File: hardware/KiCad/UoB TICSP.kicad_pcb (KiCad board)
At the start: 4 copper layers, 80 x 40 mm, 57 parts, among them J1 Wago 233-503, J2 SMA, J3 PT02A12-4PW, J4 Wago 233-506, U1 LT3045EDD, U2 LT3094EDD, U3 OPA818IDRG, U4 OPA1632DGN, U5 LT3045EDD

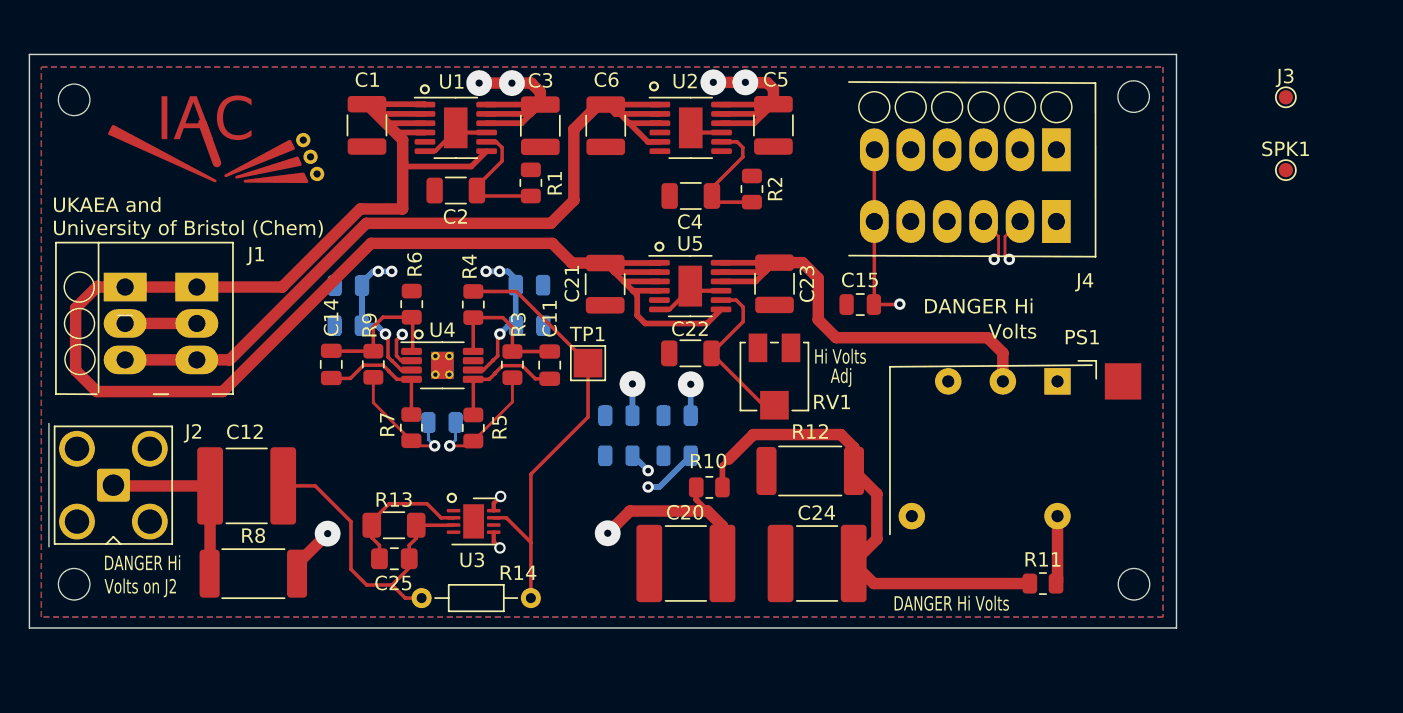
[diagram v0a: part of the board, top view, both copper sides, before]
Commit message: End of day save. Just needs voids added to planes to reduce capacitance
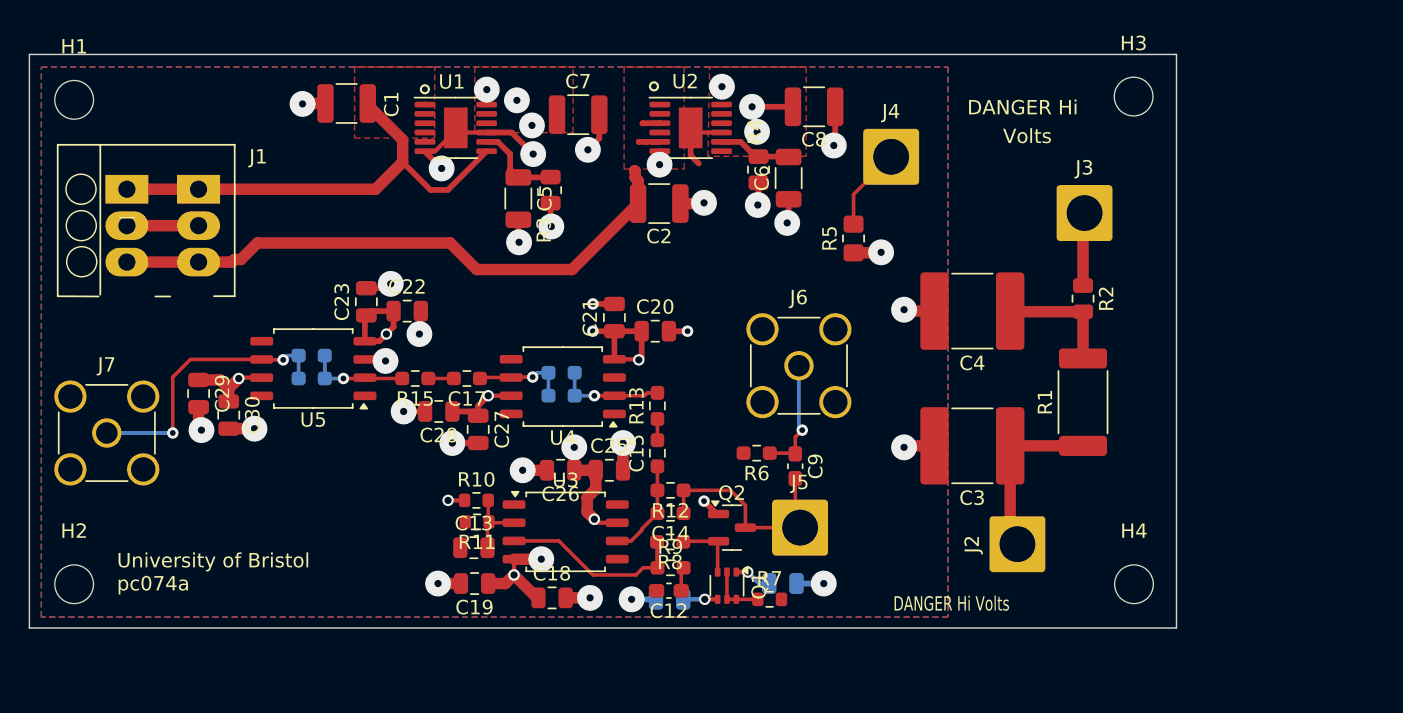
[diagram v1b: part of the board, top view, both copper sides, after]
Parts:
- removed IAC: IAC Logo, UoB Cremat Library:IAC Logo
- removed PS1: XP-Q25-5, UoB Cremat Library:XP-Q25-5 DCtoHDC
- removed RV1: 50k 3314J-2-503E, Potentiometer_SMD:Potentiometer_Bourns_3314J_Vertical
- removed SPK1: SPS-2220-03, TestPoint:TestPoint_Pad_D1.0mm
- removed TP1: TestPoint, TestPoint:TestPoint_Pad_2.0x2.0mm
- added C26: 10uF, Capacitor_SMD:C_0805_2012Metric, F.Cu at (121.0, 84.0)
- added C27: 0.1uF, Capacitor_SMD:C_0805_2012Metric, F.Cu at (115.3, 81.2)
- added C28: 10uF, Capacitor_SMD:C_0805_2012Metric, F.Cu at (112.5, 79.9)
- added C29: 0.1uF, Capacitor_SMD:C_0805_2012Metric, F.Cu at (95.8, 78.7)
- added C30: 10uF, Capacitor_SMD:C_0805_2012Metric, F.Cu at (97.9, 80.2)
- added J5: Conn_01x01_Pin, Connector_Wire:SolderWire-2sqmm_1x01_D2mm_OD3.9mm, F.Cu at (137.8, 88.0)
- added J6: SMA, Connector_Coaxial:SMA_Amphenol_901-144_Vertical, F.Cu at (137.7, 76.7)
- added J7: SMA, Connector_Coaxial:SMA_Amphenol_901-144_Vertical, F.Cu at (89.4, 81.4)
- added Q1: MMDT3906, Package_TO_SOT_SMD:SOT-363_SC-70-6, F.Cu at (132.7, 92.0)
- added Q2: 2SK932, Package_TO_SOT_SMD:SOT-23, F.Cu at (133.0, 88.0)
- added R15: 510, Resistor_SMD:R_0603_1608Metric_Pad0.98x0.95mm_HandSolder, F.Cu at (110.9, 77.6)
- added R16: 10k, Resistor_SMD:R_0603_1608Metric_Pad0.98x0.95mm_HandSolder, B.Cu at (103.7, 76.0)
- C11: value 1nF -> 10uF; moved to B.Cu
- C12: value 0.01uF C2220C103KHRACTU -> 1nF; footprint Capacitor_SMD:C_2220_5650Metric -> Capacitor_SMD:C_0603_1608Metric_Pad1.08x0.95mm_HandSolder
- C13: value 2.7nF -> 0.1uF; moved to F.Cu
- C14: value 1nF -> 10p; footprint Capacitor_SMD:C_0805_2012Metric -> Resistor_SMD:R_0603_1608Metric_Pad0.98x0.95mm_HandSolder
- C15: value 0.1uF -> 1n; footprint Capacitor_SMD:C_0805_2012Metric -> Resistor_SMD:R_0603_1608Metric_Pad0.98x0.95mm_HandSolder
- C16: value 10uF -> 50p; footprint Capacitor_SMD:C_0805_2012Metric -> Resistor_SMD:R_0603_1608Metric_Pad0.98x0.95mm_HandSolder
- C17: value 10uF -> 1n; footprint Capacitor_SMD:C_0805_2012Metric -> Resistor_SMD:R_0603_1608Metric_Pad0.98x0.95mm_HandSolder; moved to F.Cu
- C18: moved to F.Cu
- C19: value 0.1uF -> 10uF; moved to F.Cu
- C2: value 0.47uF -> 10uF C1210C106K3PACTU; footprint Capacitor_SMD:C_1206_3216Metric -> Capacitor_SMD:C_1210_3225Metric
- C20: value 0.01uF C2220C103KHRACTU -> 0.1uF; footprint Capacitor_SMD:C_2220_5650Metric -> Capacitor_SMD:C_0805_2012Metric
- C21, C23: value 10uF C1210C106K3PACTU -> 10uF; footprint Capacitor_SMD:C_1210_3225Metric -> Capacitor_SMD:C_0805_2012Metric
- C22: value 0.47uF -> 0.1uF; footprint Capacitor_SMD:C_1206_3216Metric -> Capacitor_SMD:C_0805_2012Metric
- C24: value 0.01uF C2220C103KHRACTU -> 50p; footprint Capacitor_SMD:C_2220_5650Metric -> Resistor_SMD:R_0603_1608Metric_Pad0.98x0.95mm_HandSolder; moved to B.Cu
- C25: value 0.5pF CQ0805BRNPO0BNR50 -> 0.1uF; footprint Capacitor_SMD:C_0805_2012Metric_Pad1.18x1.45mm_HandSolder -> Capacitor_SMD:C_0805_2012Metric
- C3: value 10uF C1210C106K3PACTU -> 0.01uF C2220C103KHRACTU; footprint Capacitor_SMD:C_1210_3225Metric -> Capacitor_SMD:C_2220_5750Metric_Pad1.97x5.40mm_HandSolder
- C4: value 4.7uF -> 0.01uF C2220C103KHRACTU; footprint Capacitor_SMD:C_1206_3216Metric -> Capacitor_SMD:C_2220_5750Metric_Pad1.97x5.40mm_HandSolder
- C5: value 10uF C1210C106K3PACTU -> 0.47uF; footprint Capacitor_SMD:C_1210_3225Metric -> Capacitor_SMD:C_1206_3216Metric
- C6: value 10uF C1210C106K3PACTU -> 4.7uF; footprint Capacitor_SMD:C_1210_3225Metric -> Capacitor_SMD:C_1206_3216Metric
- C7: value 10uF -> 10uF C1210C106K3PACTU; footprint Capacitor_SMD:C_0805_2012Metric -> Capacitor_SMD:C_1210_3225Metric; moved to F.Cu
- C8: value 0.1uF -> 10uF C1210C106K3PACTU; footprint Capacitor_SMD:C_0805_2012Metric -> Capacitor_SMD:C_1210_3225Metric; moved to F.Cu
- C9: value 10uF -> 1pF; footprint Capacitor_SMD:C_0805_2012Metric -> Capacitor_SMD:C_0603_1608Metric_Pad1.08x0.95mm_HandSolder; moved to F.Cu
- H1, H2, H3, H4: footprint MountingHole:MountingHole_2.2mm_M2_DIN965 -> MountingHole:MountingHole_2.7mm_M2.5
- J2: value SMA -> Conn_01x01_Pin; footprint Connector_Coaxial:SMA_Amphenol_901-143_Horizontal -> Connector_Wire:SolderWire-2sqmm_1x01_D2mm_OD3.9mm
- J3: value PT02A12-4PW -> Conn_01x01_Pin; footprint TestPoint:TestPoint_Pad_D1.0mm -> Connector_Wire:SolderWire-2sqmm_1x01_D2mm_OD3.9mm
- J4: value Wago 233-506 -> Conn_01x01_Pin; footprint UoB Cremat Library:TerminalBlock_WAGO_233-506_1x06_P2.54mm_45Degree -> Connector_Wire:SolderWire-2sqmm_1x01_D2mm_OD3.9mm
- R1: value 60k -> 200M CRHA2510AF200MFKEF; footprint Resistor_SMD:R_0805_2012Metric -> Resistor_SMD:R_2512_6332Metric_Pad1.40x3.35mm_HandSolder
- R10: value 10M RCV080510M0FKEA -> 1k; footprint Resistor_SMD:R_0805_2012Metric -> Resistor_SMD:R_0603_1608Metric
- R11: value 1 KTR10EZPF1R00 -> 1k; footprint Resistor_SMD:R_0805_2012Metric -> Resistor_SMD:R_0603_1608Metric
- R12: value 200M CRHA2510AF200MFKEF -> 2.2M; footprint Resistor_SMD:R_2512_6332Metric_Pad1.40x3.35mm_HandSolder -> Resistor_SMD:R_0603_1608Metric_Pad0.98x0.95mm_HandSolder
- R13: value 100M CRCW1206100MJPEAHR -> 510; footprint Resistor_SMD:R_1206_3216Metric_Pad1.30x1.75mm_HandSolder -> Resistor_SMD:R_0603_1608Metric_Pad0.98x0.95mm_HandSolder
- R14: value nf -> 10k; footprint Resistor_THT:R_Axial_DIN0204_L3.6mm_D1.6mm_P7.62mm_Horizontal -> Resistor_SMD:R_0603_1608Metric_Pad0.98x0.95mm_HandSolder; moved to B.Cu
- R2: value 60k -> 10M RCV080510M0FKEA
- R3, R4: value 390 -> 60k
- R5: value 40 -> 10k; footprint Resistor_SMD:R_0805_2012Metric -> Resistor_SMD:R_0805_2012Metric_Pad1.20x1.40mm_HandSolder
- R6: value 390 -> 51R; footprint Resistor_SMD:R_0805_2012Metric -> Resistor_SMD:R_0603_1608Metric_Pad0.98x0.95mm_HandSolder
- R7: value 40 -> 560; footprint Resistor_SMD:R_0805_2012Metric -> Resistor_SMD:R_0603_1608Metric
- R8: value 200M CRHA2510AF200MFKEF -> 100; footprint Resistor_SMD:R_2512_6332Metric_Pad1.40x3.35mm_HandSolder -> Resistor_SMD:R_0603_1608Metric_Pad0.98x0.95mm_HandSolder
- R9: value 390 -> 100; footprint Resistor_SMD:R_0805_2012Metric -> Resistor_SMD:R_0603_1608Metric_Pad0.98x0.95mm_HandSolder
- U3: value OPA818IDRG -> OPA891; footprint Package_SON:WSON-8-1EP_3x3mm_P0.5mm_EP1.45x2.4mm -> Package_SO:SOIC-8_5.275x5.275mm_P1.27mm
- U4: value OPA1632DGN -> OPA891; footprint Package_SO:HVSSOP-8-1EP_3x3mm_P0.65mm_EP1.57x1.89mm_ThermalVias -> Package_SO:SOIC-8_5.275x5.275mm_P1.27mm
- U5: value LT3045EDD -> OPA891; footprint Package_SO:MSOP-12-1EP_3x4mm_P0.65mm_EP1.65x2.85mm -> Package_SO:SOIC-8_5.275x5.275mm_P1.27mm
- moved J2 63.2 mm to (152.9, 89.2)
- moved R1 41.4 mm to (157.5, 79.2)
- moved R11 39.7 mm to (115.2, 87.6), turned to 180 degrees
- moved C24 37.5 mm to (103.7, 77.6), turned to 180 degrees
- moved C3 37.5 mm to (149.8, 82.3), turned to 180 degrees
- moved C10 35.2 mm to (136.6, 91.9), turned to 0 degrees
- moved C9 33.6 mm to (137.4, 83.7), turned to -90 degrees
- moved C12 30.3 mm to (128.6, 92.4)
- moved R5 29.6 mm to (141.5, 67.8)
- moved R8 29.2 mm to (128.7, 89.0), turned to 180 degrees
- moved C23 28.5 mm to (107.5, 72.2), turned to 90 degrees
- moved R7 27.7 mm to (135.6, 93.0), turned to 0 degrees
- moved U5 26.9 mm to (103.8, 76.9), turned to 180 degrees
- moved R6 26.2 mm to (134.7, 82.8), turned to 180 degrees
- moved C8 26.1 mm to (138.7, 58.6)
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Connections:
- C11 pad 1: Net-(U4-+) -> /+6V
- C11 pad 2: Net-(C11-Pad2) -> GND
- C12 pad 1: Net-(U3--) -> Net-(C12-Pad1)
- C12 pad 2: Net-(J2-In) -> GND
- C13 pad 1: /Vo- -> GND
- C13 pad 2: /Vo+ -> /CSA Core/vmid
- C14 pad 1: Net-(U4--) -> /qin
- C14 pad 2: Net-(C14-Pad2) -> /CSA Core/vfb
- C15 pad 1: GND -> /CSA Core/vfb
- C15 pad 2: /Vocm -> Net-(C15-Pad2)
- C16 pad 1: /-6V -> Net-(U4--)
- C16 pad 2: GND -> Net-(C16-Pad2)
- C17 pad 1: /-6V -> Net-(C16-Pad2)
- C17 pad 2: GND -> Net-(C17-Pad2)
- C2 pad 1: Net-(U1-SET) -> GND
- C2 pad 2: GND -> /-9V
- C20 pad 1: Net-(C20-Pad1) -> /-6V
- C21 pad 1: /+9V -> /-6V
- C22 pad 1: Net-(U5-SET) -> /-6V
- C23 pad 1: /+1-5V HiVip -> /-6V
- C24 pad 1: GND -> Net-(U5--)
- C24 pad 2: /Bias 500 - 2500V -> /vout
- C25 pad 1: Net-(U3-FB) -> /+6V
- C25 pad 2: Net-(U3--) -> GND
- C3 pad 1: /+6V -> /detector_bias
- C4 pad 1: GND -> /bias_filt
- C4 pad 2: Net-(U2-SET) -> GND
- C5 pad 1: GND -> Net-(U1-SET)
- C5 pad 2: /-6V -> GND
- C6 pad 2: /-9V -> Net-(U2-SET)
- C8 pad 1: /+6V -> GND
- C8 pad 2: GND -> /-6V
- C9 pad 1: /+6V -> Net-(J6-In)
- C9 pad 2: GND -> /qin
- J2 pad 1: Net-(J2-In) -> /detector_bias
- J3 pad 1: unconnected-(J3-Pad1) -> /bias_in
- J4 pad 1: /Vo- -> Net-(J4-Pin_1)
- R1 pad 1: Net-(U1-SET) -> /detector_bias
- R1 pad 2: GND -> /bias_filt
- R10 pad 1: /Bias 500 - 2500V -> /+6V
- R10 pad 2: Net-(C20-Pad1) -> /CSA Core/vmid
- R11 pad 1: /Bias 500 - 2500V -> /CSA Core/vmid
- R11 pad 2: Net-(PS1-+HV) -> GND
- R12 pad 1: /Bias 500 - 2500V -> /qin
- R12 pad 2: GND -> /CSA Core/vfb
- R13 pad 1: Net-(U3-FB) -> Net-(C15-Pad2)
- R13 pad 2: Net-(U3--) -> Net-(U4--)
- R14 pad 1: Net-(R14-Pad1) -> Net-(U4--)
- R14 pad 2: Net-(U3--) -> Net-(C16-Pad2)
- R2 pad 1: GND -> /bias_in
- R2 pad 2: Net-(U2-SET) -> /bias_filt
- R3 pad 1: /Vo- -> Net-(U1-SET)
- R3 pad 2: Net-(U4-+) -> GND
- R4 pad 1: Net-(U4-+) -> GND
- R4 pad 2: Net-(R14-Pad1) -> Net-(U2-SET)
- R5 pad 1: /Vo- -> GND
- R5 pad 2: Net-(C11-Pad2) -> Net-(J4-Pin_1)
- R6 pad 1: Net-(U4--) -> Net-(J6-In)
- R7 pad 1: /Vo+ -> /CSA Core/mirror_base
- R7 pad 2: Net-(C14-Pad2) -> GND
- R8 pad 1: Net-(J2-In) -> /CSA Core/vfet
- R8 pad 2: Net-(C20-Pad1) -> /CSA Core/vbuf
- R9 pad 1: /Vo+ -> /CSA Core/vbuf
- R9 pad 2: Net-(U4--) -> Net-(C12-Pad1)
- U3 pad 2: Net-(U3-FB) -> /CSA Core/vmid
- U3 pad 3: Net-(U3--) -> /CSA Core/vbuf
- U3 pad 4: GND -> /-6V
- U3 pad 5: /-6V -> unconnected-(U3-Pad5)
- U3 pad 6: unconnected-(U3-NC-Pad6) -> /CSA Core/vfb
- U3 pad 7: Net-(R14-Pad1) -> /+6V
- U3 pad 8: /+6V -> unconnected-(U3-NULL2-Pad8)
- U4 pad 1: Net-(U4--) -> unconnected-(U4-NULL1-Pad1)
- U4 pad 2: /Vocm -> Net-(U4--)
- U4 pad 3: /+6V -> GND
- U4 pad 4: Net-(C14-Pad2) -> /-6V
- U4 pad 5: Net-(C11-Pad2) -> unconnected-(U4-Pad5)
- U4 pad 6: /-6V -> Net-(C16-Pad2)
- U4 pad 7: unconnected-(U4-Enable-Pad7) -> /+6V
- U4 pad 8: Net-(U4-+) -> unconnected-(U4-NULL2-Pad8)
- U5 pad 1: /+9V -> unconnected-(U5-NULL1-Pad1)
- U5 pad 2: /+9V -> Net-(U5--)
- U5 pad 3: /+9V -> GND
- U5 pad 4: /+9V -> /-6V
- U5 pad 6: GND -> /vout
- U5 pad 7: /+9V -> /+6V
- U5 pad 8: Net-(U5-SET) -> unconnected-(U5-NULL2-Pad8)
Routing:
- net /+9V: track 128.7 -> 38.9 mm
- net /Vo+: track 69.0 -> 0.00 mm, vias 2 -> 0
- net /Vo-: track 69.0 -> 0.00 mm, vias 2 -> 0
- net /Vocm: track 51.0 -> 0.00 mm, vias 2 -> 0
- net GND: track 23.0 -> 70.0 mm, vias 0 -> 30
- net Net-(C20-Pad1): track 36.9 -> 0.00 mm, vias 2 -> 0
- net /Bias 500 - 2500V: track 34.2 -> 0.00 mm
- net /+1-5V HiVip: track 34.2 -> 0.00 mm
- net Net-(R14-Pad1): track 31.4 -> 0.00 mm
- net Net-(U3--): track 22.3 -> 0.00 mm
- net /vout: track 0.00 -> 19.5 mm, vias 0 -> 2
- net /qin: track 0.00 -> 15.3 mm
- net /-9V: track 58.6 -> 44.0 mm
- net /CSA Core/vbuf: track 0.00 -> 13.0 mm
- net Net-(J2-In): track 12.9 -> 0.00 mm
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- added copper zone on F.Cu, net /+6V
- added copper zone on In2.Cu, net /+6V
- added copper zone on F.Cu, net /+9V
- added copper zone on B.Cu, net /-6V
- added copper zone on F.Cu, net /-6V
- added copper zone on F.Cu, net /-9V
- added copper zone on In1.Cu, net GND
- removed copper zone on In1.Cu, net /+6V
- removed copper zone on In2.Cu, net /-6V
- removed copper zone on B.Cu, net GND
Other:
- board text added: "University of Bristol pc074a"
- board text removed: "Adj"
- board text removed: "Hi Volts"
- board text removed: "UKAEA and University of Bristol (Chem)"
- board text removed: "Volts on J2"

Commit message: Generated artwork
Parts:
- removed U1: LT3045EDD, Package_SO:MSOP-12-1EP_3x4mm_P0.65mm_EP1.65x2.85mm
- removed U2: LT3094EDD, Package_SO:MSOP-12-1EP_3x4mm_P0.65mm_EP1.65x2.85mm
- added C31: 0.1uF, Capacitor_SMD:C_0805_2012Metric, F.Cu at (137.3, 90.1)
- added L1: Wurth 742792651, Inductor_SMD:L_0603_1608Metric_Pad1.05x0.95mm_HandSolder, B.Cu at (129.8, 90.0)
- added R17: 240, Resistor_SMD:R_0603_1608Metric_Pad0.98x0.95mm_HandSolder, F.Cu at (107.2, 59.1)
- added R18: 240, Resistor_SMD:R_0603_1608Metric_Pad0.98x0.95mm_HandSolder, B.Cu at (127.7, 60.4)
- added R19: 1k, Resistor_SMD:R_0603_1608Metric_Pad0.98x0.95mm_HandSolder, F.Cu at (134.8, 91.8)
- added R20: 1k, Resistor_SMD:R_0603_1608Metric_Pad0.98x0.95mm_HandSolder, F.Cu at (131.8, 91.7)
- added R21: 10, Resistor_SMD:R_0603_1608Metric_Pad0.98x0.95mm_HandSolder, B.Cu at (132.7, 89.2)
- added U6: LM317_SOT-223, Package_TO_SOT_SMD:SOT-223-3_TabPin2, F.Cu at (113.7, 60.2)
- added U7: LM337_SOT223, Package_TO_SOT_SMD:SOT-223-3_TabPin2, F.Cu at (133.7, 60.1)
- C12: value 1nF -> 1n
- C16, C24: value 50p -> 47p
- C5: value 0.47uF -> 10uF C1210C106K3PACTU; footprint Capacitor_SMD:C_1206_3216Metric -> Capacitor_SMD:C_1210_3225Metric
- C6: value 4.7uF -> 10uF C1210C106K3PACTU; footprint Capacitor_SMD:C_1206_3216Metric -> Capacitor_SMD:C_1210_3225Metric
- Q1: value MMDT3906 -> BFS20; footprint Package_TO_SOT_SMD:SOT-363_SC-70-6 -> Package_TO_SOT_SMD:SOT-23
- R10: footprint Resistor_SMD:R_0603_1608Metric -> Resistor_SMD:R_0603_1608Metric_Pad0.98x0.95mm_HandSolder
- R11: value 1k -> 1.5k; footprint Resistor_SMD:R_0603_1608Metric -> Resistor_SMD:R_0603_1608Metric_Pad0.98x0.95mm_HandSolder
- R3: value 60k -> 1.8k; footprint Resistor_SMD:R_0805_2012Metric -> Resistor_SMD:R_0603_1608Metric_Pad0.98x0.95mm_HandSolder
- R4: value 60k -> 1k; footprint Resistor_SMD:R_0805_2012Metric -> Resistor_SMD:R_0603_1608Metric_Pad0.98x0.95mm_HandSolder
- R5: value 10k -> 1k; footprint Resistor_SMD:R_0805_2012Metric_Pad1.20x1.40mm_HandSolder -> Resistor_SMD:R_0603_1608Metric_Pad0.98x0.95mm_HandSolder
- R7: value 560 -> 1.2k; footprint Resistor_SMD:R_0603_1608Metric -> Resistor_SMD:R_0603_1608Metric_Pad0.98x0.95mm_HandSolder
- R8: value 100 -> 1k
- R9: value 100 -> 10
- moved C6 33.4 mm to (104.0, 58.0), turned to 180 degrees
- moved R3 16.1 mm to (104.6, 61.2), turned to 180 degrees
- moved C8 12.5 mm to (129.0, 66.5), turned to 0 degrees
- moved C5 10.1 mm to (125.5, 58.2), turned to 0 degrees
- moved R4 9.07 mm to (126.1, 60.7), turned to 0 degrees
- moved C2 8.81 mm to (136.5, 67.4), turned to 90 degrees
- moved C1 5.99 mm to (106.5, 64.4)
- moved C7 5.73 mm to (120.3, 64.6), turned to -90 degrees
- moved R6 5.23 mm to (138.9, 79.7), turned to 0 degrees
- moved Q1 3.72 mm to (133.0, 88.3), turned to 180 degrees
- moved J5 3.31 mm to (137.7, 84.7)
- moved C9 3.26 mm to (136.5, 80.6)
- moved Q2 3.11 mm to (133.1, 84.9)
- moved R7 2.71 mm to (133.2, 91.7), turned to 90 degrees
- moved J6 2.37 mm to (136.6, 74.6)
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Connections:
- net /+9V renamed /+12V
- net /-6V renamed /V-
- C10 pad 1: /+6V -> Net-(C10-Pad1)
- C11 pad 1: /+6V -> Net-(C10-Pad1)
- C25 pad 1: /+6V -> /+10V
- C26 pad 1: /+6V -> /+10V
- C27 pad 1: /+6V -> /+10V
- C28 pad 1: /+6V -> /+10V
- C29 pad 1: /+6V -> /+10V
- C30 pad 1: /+6V -> /+10V
- C5 pad 1: Net-(U1-SET) -> GND
- C5 pad 2: GND -> Net-(U7-ADJ)
- C6 pad 1: GND -> Net-(U6-ADJ)
- C6 pad 2: Net-(U2-SET) -> GND
- C7 pad 1: /+6V -> /+10V
- Q1 pad 1: /+6V -> /CSA Core/vbase
- Q1 pad 2: /CSA Core/mirror_base -> /CSA Core/ve
- Q1 pad 3: /CSA Core/vfet -> /CSA Core/vc
- Q2 pad 2: /CSA Core/vfet -> /CSA Core/ve
- R10 pad 1: /+6V -> /+10V
- R3 pad 1: Net-(U1-SET) -> Net-(U6-ADJ)
- R4 pad 2: Net-(U2-SET) -> Net-(U7-ADJ)
- R7 pad 1: /CSA Core/mirror_base -> Net-(C10-Pad1)
- R7 pad 2: GND -> /CSA Core/vbase
- R8 pad 1: /CSA Core/vfet -> /CSA Core/vc
- U3 pad 7: /+6V -> /+10V
- U4 pad 7: /+6V -> /+10V
- U5 pad 7: /+6V -> /+10V
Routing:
- net /+10V: track 0.00 -> 35.4 mm, vias 0 -> 9
- net /+6V: track 27.2 -> 0.00 mm, vias 10 -> 0
- net /-9V: track 44.0 -> 60.6 mm
- net GND: track 70.0 -> 54.1 mm, vias 30 -> 28
- net /+12V: track 38.9 -> 23.1 mm
- net /CSA Core/vbase: track 0.00 -> 9.68 mm
- net Net-(C10-Pad1): track 0.00 -> 8.58 mm, vias 0 -> 2
- net Net-(U6-ADJ): track 0.00 -> 8.42 mm
- net Net-(U7-ADJ): track 0.00 -> 8.24 mm, vias 0 -> 1
- net /V-: track 27.9 -> 34.4 mm, vias 8 -> 7
- net Net-(U1-SET): track 6.12 -> 0.00 mm
- net /CSA Core/vc: track 0.00 -> 5.37 mm
- net Net-(U2-SET): track 5.12 -> 0.00 mm
- net /CSA Core/vfet: track 4.66 -> 0.00 mm
- net /CSA Core/mirror_base: track 4.05 -> 0.00 mm
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- added copper zone on In2.Cu, net /+10V
- removed copper zone on F.Cu, net /+12V
- removed copper zone on F.Cu, net /+6V
- removed copper zone on In2.Cu, net /+6V
- removed copper zone on F.Cu, net /-9V
- removed copper zone on F.Cu, net /V-
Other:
- board text added: "+12V"
- board text added: "-9V"
- board text added: "0V"
- board text added: "2"
- board text added: "3"
- board text added: "Amp In"
- board text added: "Amp Out"
- board text added: "B"
- board text added: "Bias In"
- board text added: "Bias Return"
- board text added: "Charge Inject"
- board text added: "Detector Bias"
- board text added: "T"
- board text removed: "Fusion Industry Programme STRIDES II UK Atomic Energy Authority and University of Bristol (Chemistry) Contract 13513 Commercial in Confidence"
